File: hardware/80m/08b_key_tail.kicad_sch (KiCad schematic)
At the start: 8 parts, among them Q406 DMN2056U-7

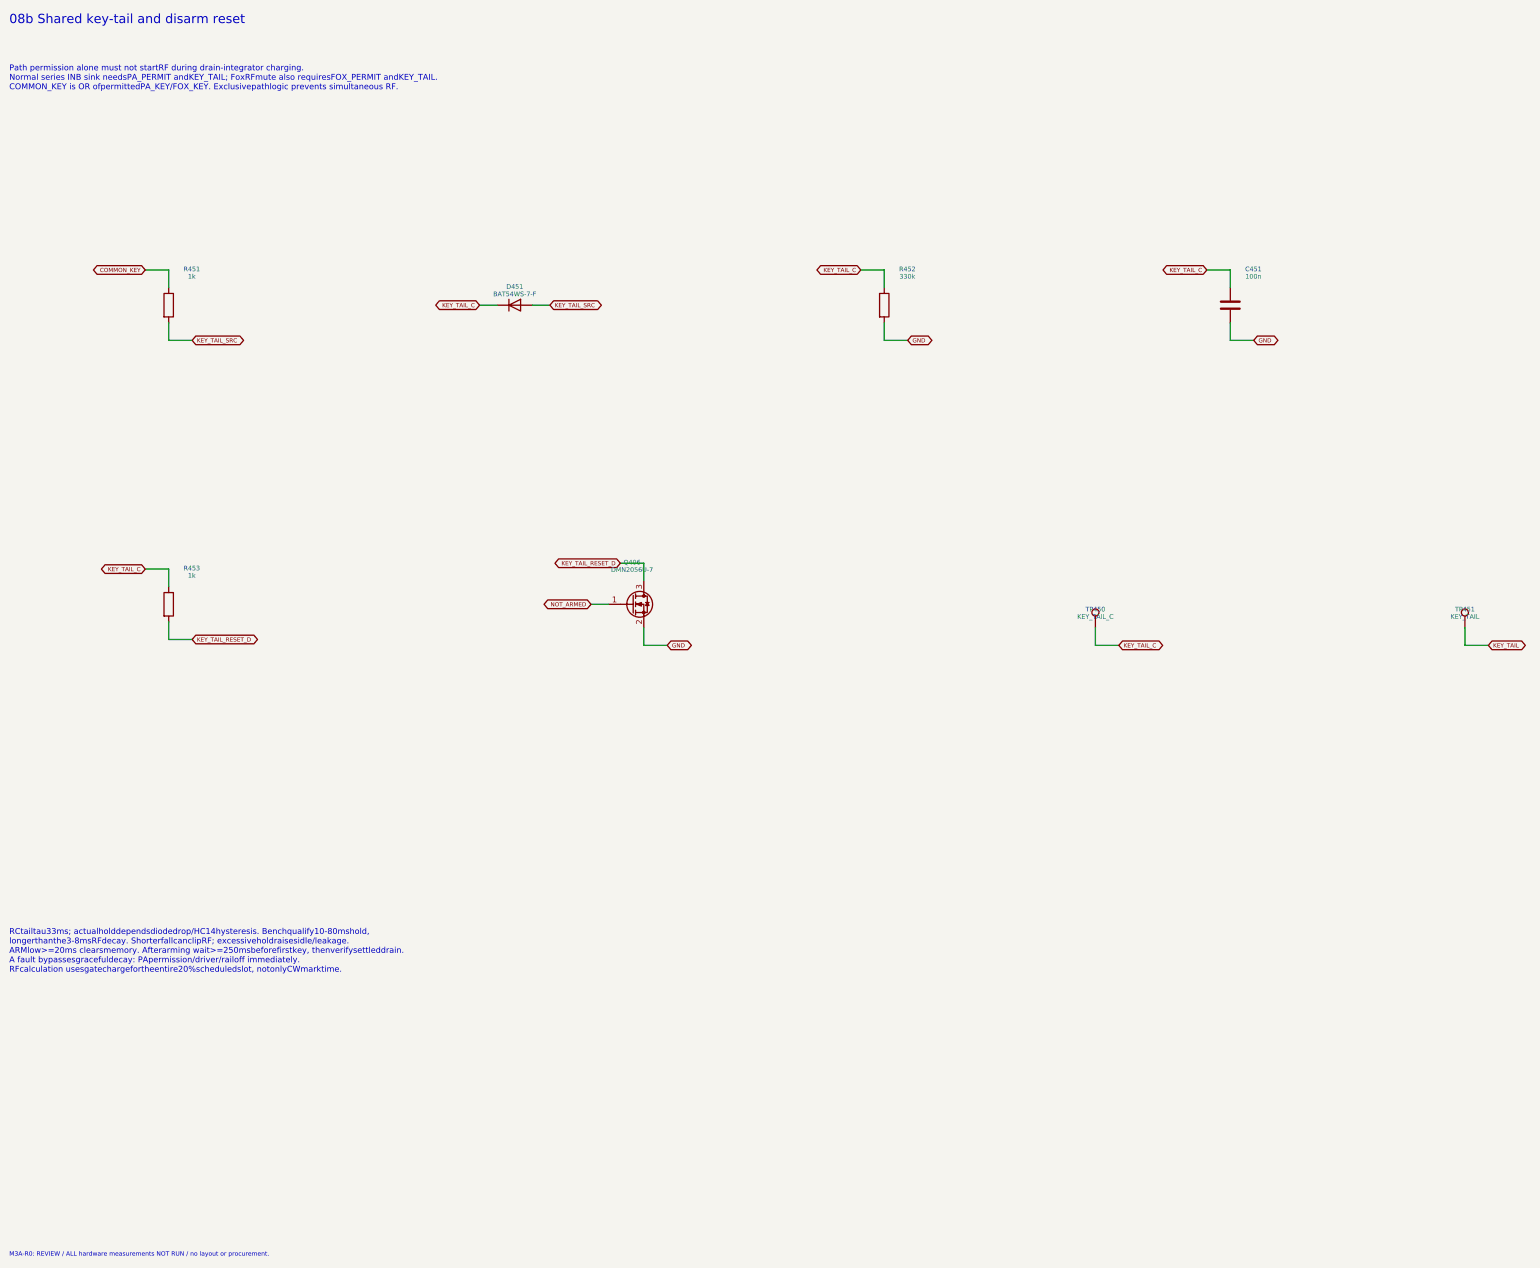
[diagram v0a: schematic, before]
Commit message: Correct RF80 timer polarities and arming logic for M3A-R1 review
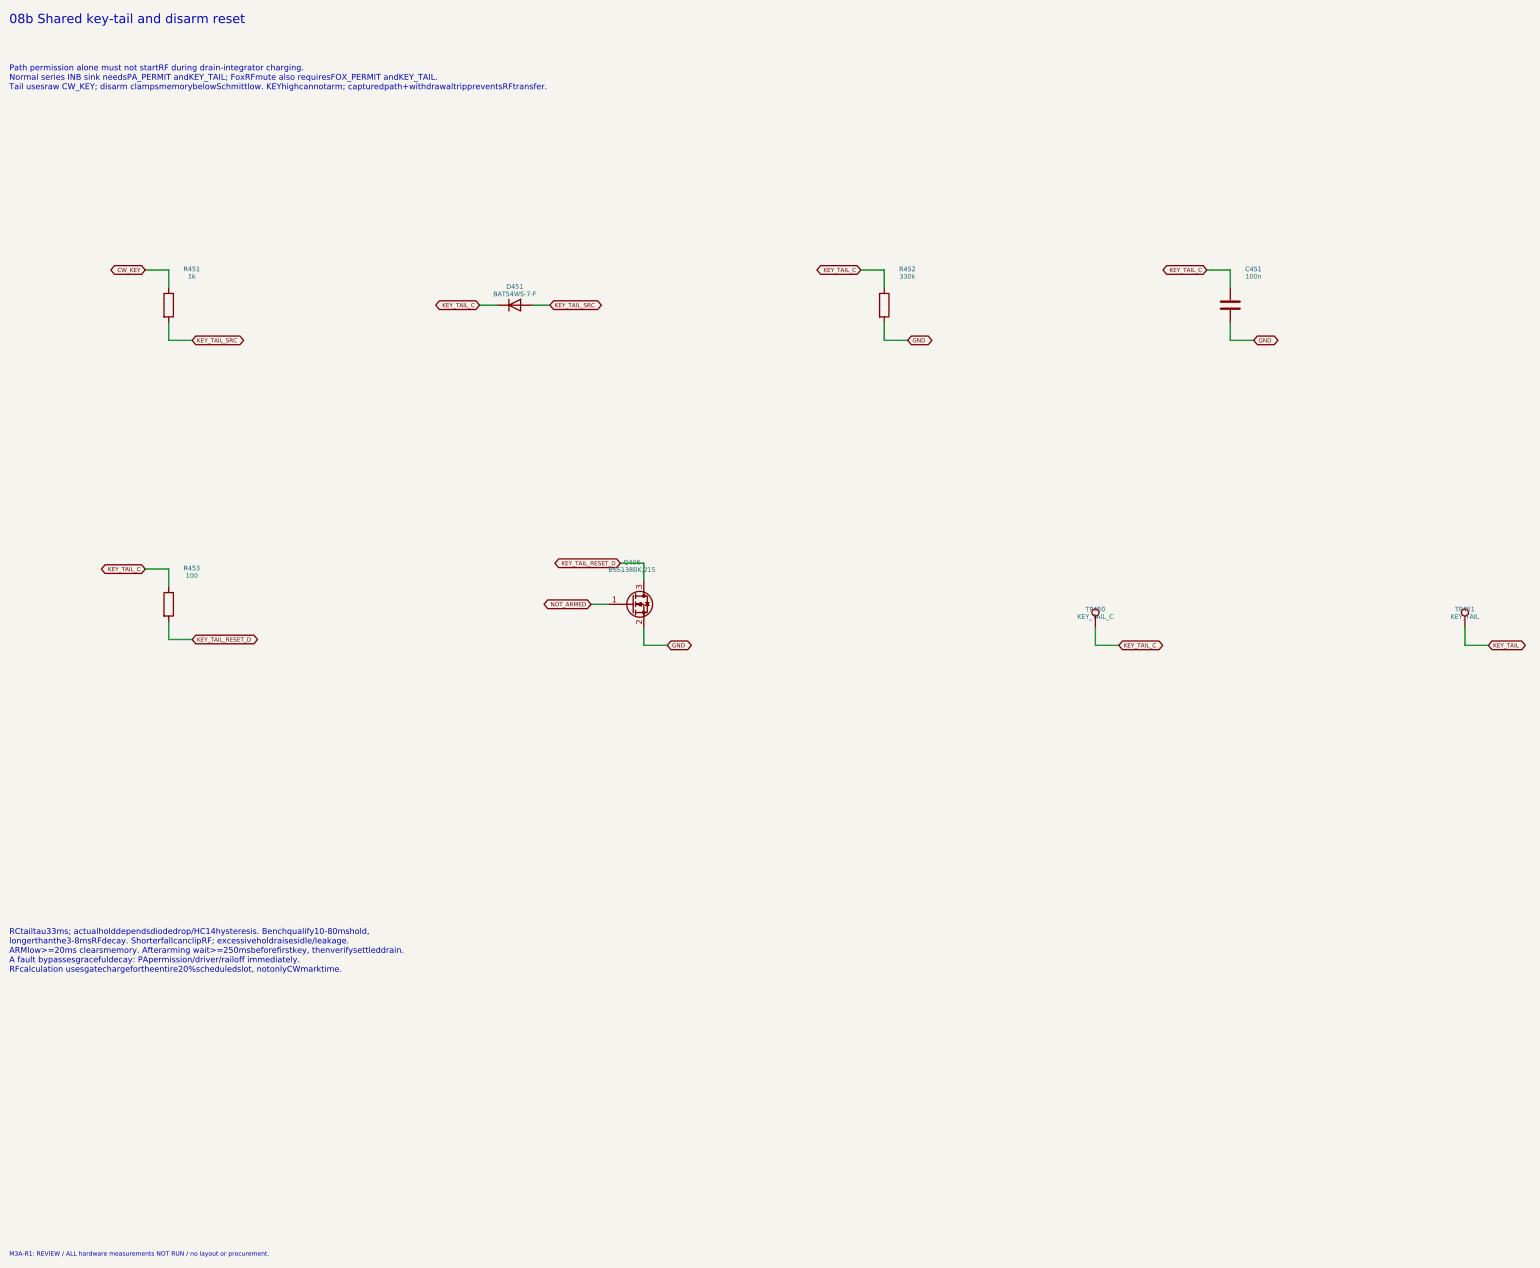
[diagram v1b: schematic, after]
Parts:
- Q406: value DMN2056U-7 -> BSS138BK,215; Engineering_Note 100usRCdischargeresetskeymemorywhileunarmed; preventsrearms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 -> 10usresetRCclampsrawKEYevenifheldhigh; KEYhighcannotarm. Ve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; MPN DMN2056U-7 -> BSS138BK,215
- R453: value 1k -> 100; MPN RC0603FR-071KL -> RC0603FR-07100RL
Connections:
- net COMMON_KEY renamed CW_KEY
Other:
- note added: "M3A-R1: REVIEW / ALL hardware measurements NOT RUN / no layout or procurement."
- note added: "Path permission alone must not startRF during drain-integrator charging. Normal series INB sink needsPA_PERMIT andKEY_TAIL; FoxRFmute also requiresFOX_PERMIT andKEY_TAIL. Tail usesraw CW_KEY; disarm clampsmemorybelowSchmittlow. KEYhighcannotarm; capturedpath+withdrawaltrippreventsRFtransfer."
- note removed: "M3A-R0: REVIEW / ALL hardware measurements NOT RUN / no layout or procurement."
- note removed: "Path permission alone must not startRF during drain-integrator charging. Normal series INB sink needsPA_PERMIT andKEY_TAIL; FoxRFmute also requiresFOX_PERMIT andKEY_TAIL. COMMON_KEY is OR ofpermittedPA_KEY/FOX_KEY. Exclusivepathlogic prevents simultaneous RF."

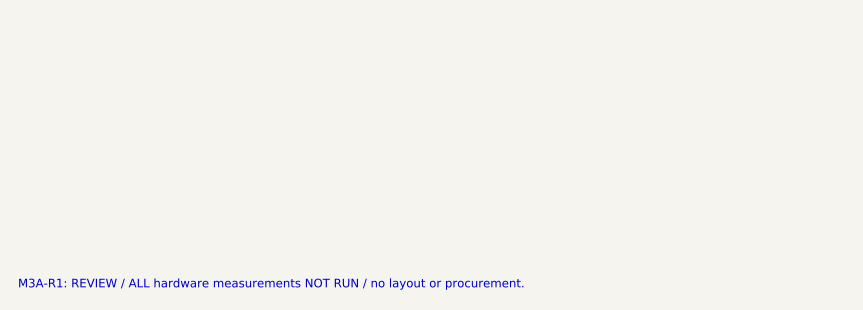
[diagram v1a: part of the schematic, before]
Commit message: Preserve M3B-E1 evaluation PCB before independent-review corrections
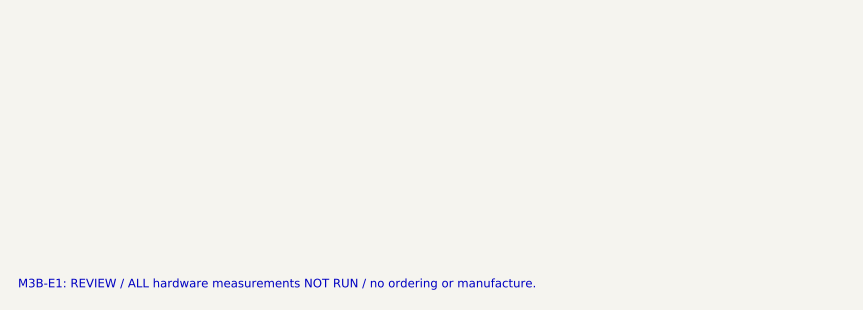
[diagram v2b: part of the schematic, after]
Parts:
- C451: Engineering_Note Dated M2 distributor observation; no fresh basket verificat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 -> (none)
- TP450, TP451: now left out of the parts list
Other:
- note added: "M3B-E1: REVIEW / ALL hardware measurements NOT RUN / no ordering or manufacture."
- note removed: "M3A-R1: REVIEW / ALL hardware measurements NOT RUN / no layout or procurement."

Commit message: Correct RF80 M3B-E2 physical pinouts and audit manufacturing readiness
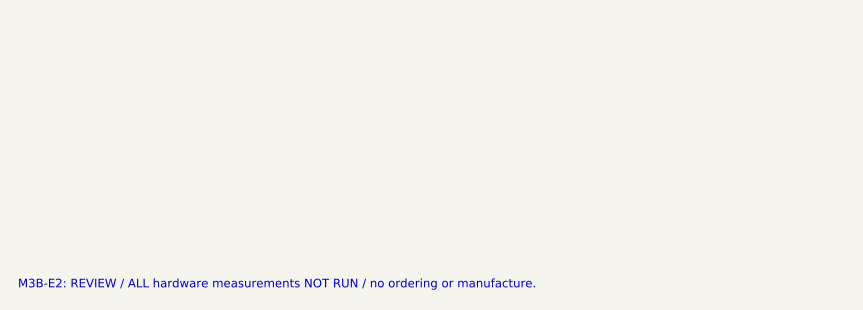
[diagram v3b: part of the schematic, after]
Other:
- note added: "M3B-E2: REVIEW / ALL hardware measurements NOT RUN / no ordering or manufacture."
- note removed: "M3B-E1: REVIEW / ALL hardware measurements NOT RUN / no ordering or manufacture."
